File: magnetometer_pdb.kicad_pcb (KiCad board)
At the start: 2 copper layers, 98 x 87.5 mm, 61 parts, among them J1 Screw_Terminal_01x02, J10 Screw_Terminal_01x02, J11 Screw_Terminal_01x02, J12 Screw_Terminal_01x02, J13 Screw_Terminal_01x02, J14 Screw_Terminal_01x02, J2 Screw_Terminal_01x02, J3 Screw_Terminal_01x02, J4 Screw_Terminal_01x02, J5 Screw_Terminal_01x02, J6 Conn_01x02_Pin, J7 Conn_01x02_Pin, J8 Conn_01x02_Pin, J9 Screw_Terminal_01x02, U1 TPS56528DDA, U2 L78L09_SO8

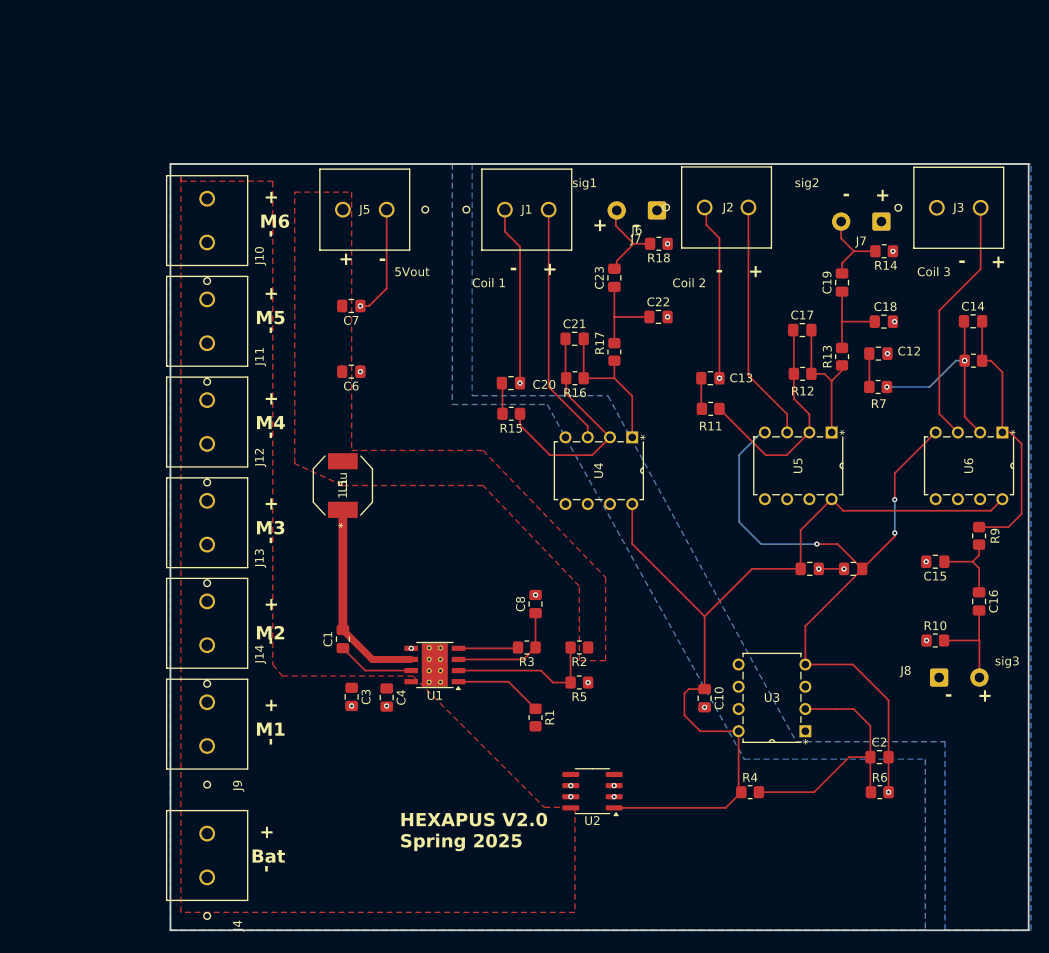
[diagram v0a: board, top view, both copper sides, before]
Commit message: changed vias
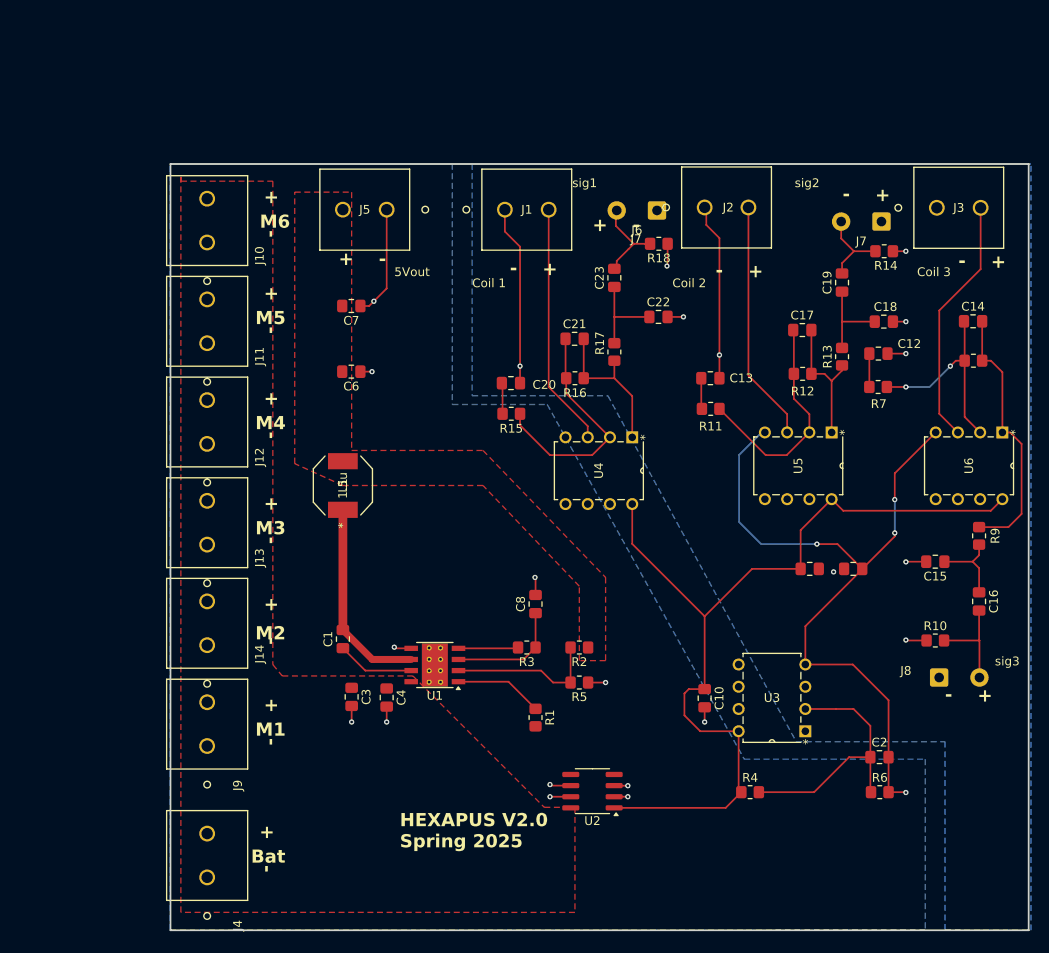
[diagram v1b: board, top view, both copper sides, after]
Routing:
- net Bat_GND: track 95.1 -> 117.6 mm
- net GND: track 43.5 -> 54.8 mm, vias 11 -> 10
- net Net-(U6--): track 23.5 -> 23.2 mm, vias 3 -> 2

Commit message: Modified schematic and pcb
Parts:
- added C11: 10u, Capacitor_SMD:C_0805_2012Metric_Pad1.18x1.45mm_HandSolder, F.Cu at (1.91, 1.00)
- added C11: 10u, Capacitor_SMD:C_0805_2012Metric_Pad1.18x1.45mm_HandSolder, F.Cu at (73.0, 87.5)
- added C24: 10u, Capacitor_SMD:C_0805_2012Metric_Pad1.18x1.45mm_HandSolder, F.Cu at (60.5, 87.9)
- added J15: Conn_01x02_Pin, Connector_PinSocket_2.54mm:PinSocket_1x02_P2.54mm_Vertical, F.Cu at (60.0, 80.7)
- added R19: 10k, Resistor_SMD:R_0805_2012Metric_Pad1.20x1.40mm_HandSolder, F.Cu at (55.5, 79.4)
- R1: value 10k -> 47k
- moved C7 27.2 mm to (38.0, 58.4), turned to 0 degrees
- moved C6 16.7 mm to (38.0, 55.4), turned to 0 degrees
- moved L1 13.2 mm to (37.4, 64.9)
- moved C10 10.5 mm to (86.0, 83.5), turned to 0 degrees
- moved C3 8.51 mm to (46.0, 79.4), turned to 0 degrees
- moved R4 8.19 mm to (92.0, 87.0)
- moved R1 7.35 mm to (52.0, 79.4)
- moved C8 6.88 mm to (55.5, 71.0), turned to 180 degrees
- moved R3 5.69 mm to (54.5, 66.0), turned to 90 degrees
- moved J5 5.29 mm to (37.0, 20.2), turned to 0 degrees
- moved C1 4.99 mm to (41.5, 71.9), turned to -90 degrees
- moved R5 4.10 mm to (64.4, 70.1)
- moved R2 3.90 mm to (64.4, 74.1)
- moved C4 3.86 mm to (46.0, 76.9), turned to 0 degrees
- moved R18 3.20 mm to (70.5, 25.5)
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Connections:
- C1 pad 1: Net-(U1-VBST) -> /5v Power Supply/BK_SW
- C1 pad 2: Net-(U1-SW) -> Net-(U1-VBST)
- C2 pad 1: Net-(U3--) -> Net-(U3-+)
- C6 pad 1: Bat_GND -> 5V_out
- C6 pad 2: 5V_out -> Bat_GND
- C7 pad 1: Bat_GND -> 5V_out
- C7 pad 2: 5V_out -> Bat_GND
- C8 pad 1: Net-(U1-VREG5) -> Bat_GND
- C8 pad 2: Bat_GND -> Net-(U1-VREG5)
- J5 pad 1: Bat_GND -> 5V_out
- J5 pad 2: 5V_out -> Bat_GND
- L1 pad 1: Net-(U1-SW) -> /5v Power Supply/BK_SW
- R1 pad 2: unconnected-(R1-Pad2) -> Vin
- R2 pad 1: 5V_out -> Bat_GND
- R4 pad 2: Net-(U3--) -> Net-(U3-+)
- R5 pad 1: Bat_GND -> 5V_out
- R6 pad 1: Net-(U3--) -> Net-(U3-+)
- U1 pad 6: Net-(U1-SW) -> /5v Power Supply/BK_SW
- U1 pad 9: unconnected-(U1-GND-Pad9) -> Bat_GND
- U3 pad 2: Net-(U3--) -> GND
- U3 pad 3: GND -> Net-(U3-+)
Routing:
- net 5V_out: track 0.00 -> 61.7 mm
- net Net-(U3--): track 30.1 -> 0.00 mm
- net Net-(U1-SW): track 22.9 -> 0.00 mm
- net (no net): track 0.00 -> 15.7 mm
- net Net-(U1-VBST): track 8.86 -> 3.68 mm
- net Net-(U1-VREG5): track 13.3 -> 8.12 mm
- net Net-(U3-+): track 0.00 -> 4.91 mm
- net 9V_out: track 101.3 -> 106.2 mm
- net Net-(J15-Pin_2): track 10.1 -> 13.6 mm
- net GND: track 54.8 -> 58.1 mm, vias 10 -> 9
- net Bat_GND: track 117.6 -> 115.3 mm, vias 16 -> 21
- net Net-(U1-PG): track 6.71 -> 8.45 mm
- net Net-(C22-Pad1): track 10.4 -> 8.94 mm
- net Coil_1_sig_out: track 9.69 -> 9.02 mm
- net Vin: vias 0 -> 1
- added copper zone on F.Cu, net /5v Power Supply/BK_SW
- added copper zone on F.Cu, net Bat_GND

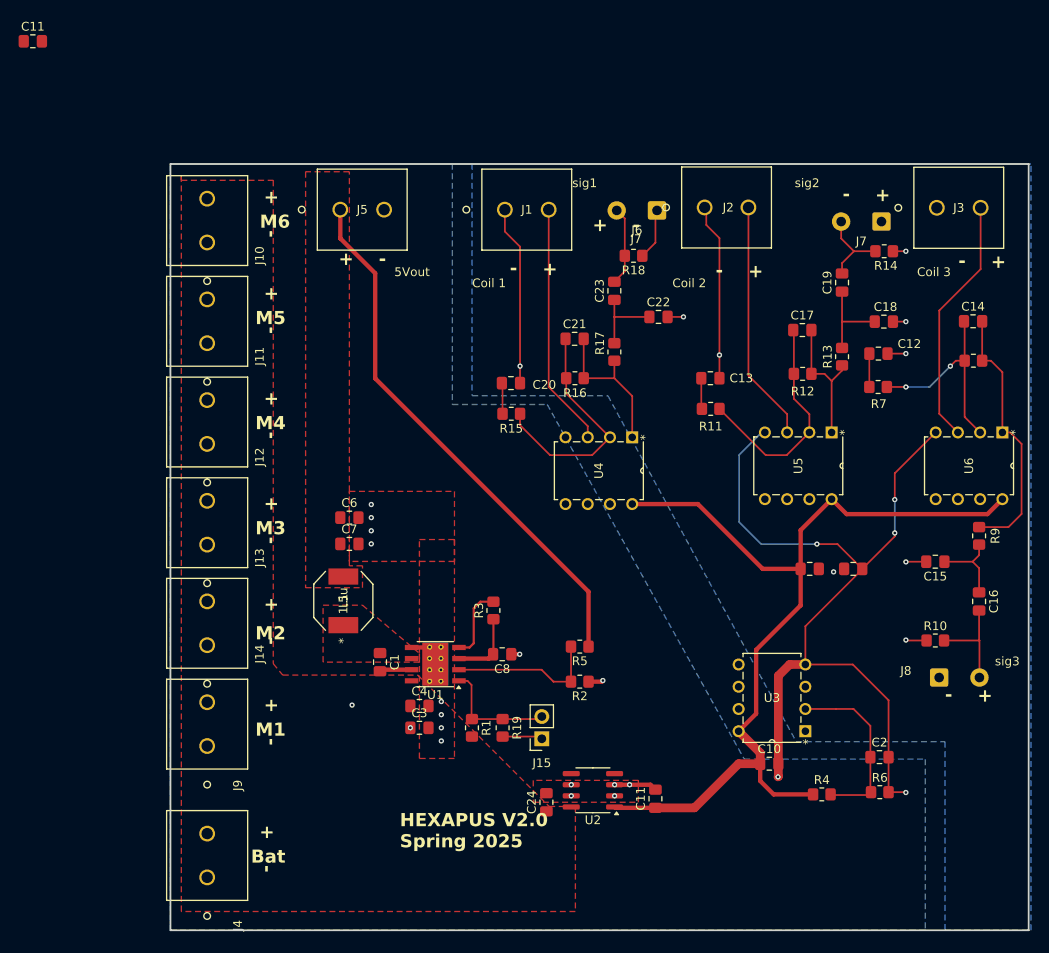
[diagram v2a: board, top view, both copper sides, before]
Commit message: Added decoupling caps
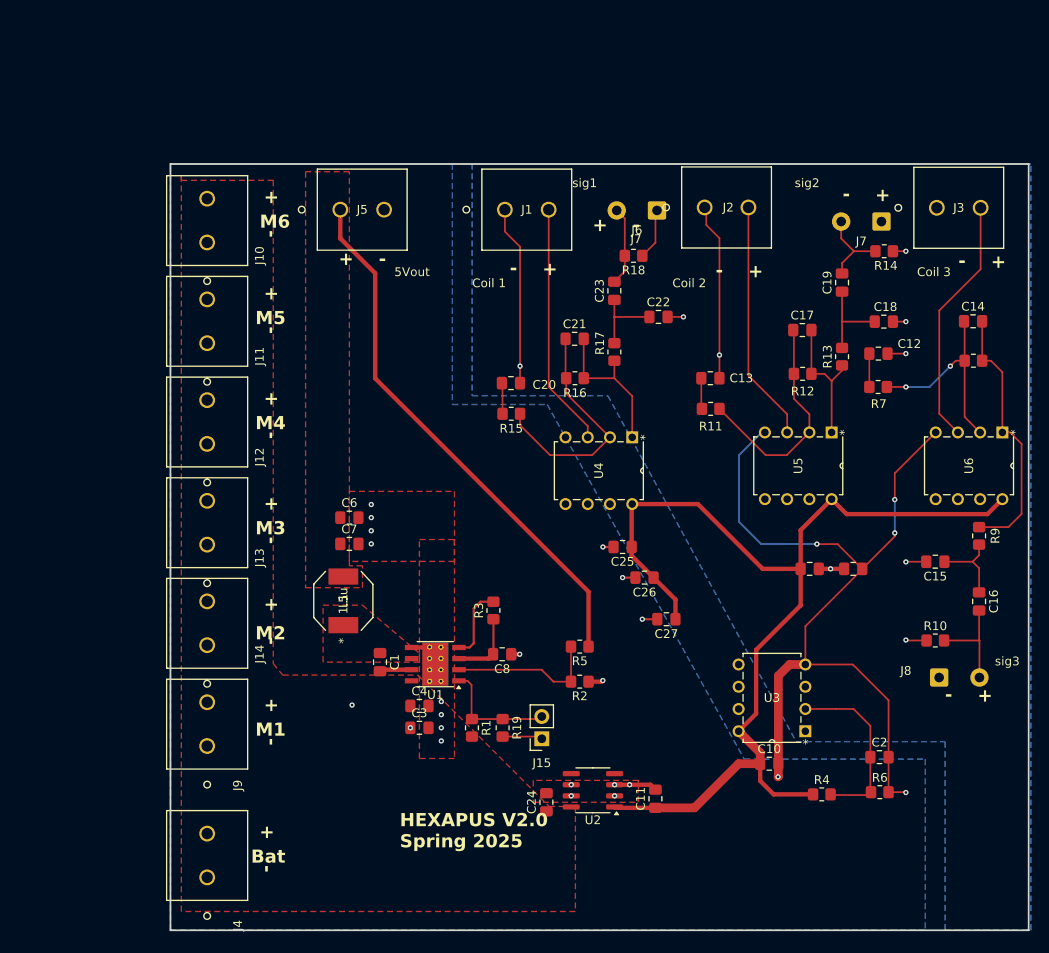
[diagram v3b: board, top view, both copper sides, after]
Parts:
- removed the C11 at (1.91, 1.00)
- added C25: 2.2u, Capacitor_SMD:C_0805_2012Metric_Pad1.18x1.45mm_HandSolder, F.Cu at (69.2, 58.8)
- added C26: 2.2u, Capacitor_SMD:C_0805_2012Metric_Pad1.18x1.45mm_HandSolder, F.Cu at (71.8, 62.2)
- added C27: 2.2u, Capacitor_SMD:C_0805_2012Metric_Pad1.18x1.45mm_HandSolder, F.Cu at (74.2, 67.0)
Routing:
- net 9V_out: track 106.2 -> 121.5 mm
- net Bat_GND: track 115.3 -> 119.7 mm, vias 21 -> 24
- net GND: track 58.1 -> 61.0 mm
